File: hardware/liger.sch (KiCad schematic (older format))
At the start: 61 parts, among them P1 CONN_01X10, P2 CONN_01X10, P3 USB_OTG, P4 CONN_01X02, P5 CONN_01X04, Q1 Q_NMOS_GSD, Q2 Q_PMOS_GSD, Q3 Q_NPN_BEC, Q4 Q_NPN_BEC, SW1 SW_PUSH, U1 electret_microphone, U11 SPX3819, U2 ADA4075, U3 ESP-WROOM-02, U4 FT230XS, U5 PT5529B/L2/H2-F

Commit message: pcbebe
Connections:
- net at Relay1.8: now also P4.1 (P1)
- net at Relay1.9: no longer P4.1 (P1)

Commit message: almost done
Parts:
- removed R19: 100 something, Resistors_SMD:R_0603, symbol R
- R18: value 100something -> 1K; Part Number (none) -> RC0603JR-071KL
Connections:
- net +3V3: now also R18.1
- net RXD: now also R18.2, U4.1 (TXD); no longer R18.1
- net TXD: now also U4.4 (RXD)
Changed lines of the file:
@@
 Text GLabel 12100 4700 2    60   Input ~ 0
 RESET
-Text GLabel 12050 3950 2    60   Input ~ 0
+Text GLabel 11900 3950 2    60   Input ~ 0
 TXD
-Text GLabel 12050 3850 2    60   Input ~ 0
+Text GLabel 11600 3850 2    60   Input ~ 0
 RXD
 $Comp
@@
 $EndComp
 $Comp
-L R R18
-U 1 1 57701A9A
-P 11750 3850
-F 0 "R18" V 11650 3850 50  0000 C CNN
-F 1 "100something" V 11750 3850 50  0000 C CNN
-F 2 "Resistors_SMD:R_0603" V 11680 3850 50  0001 C CNN
-F 3 "" H 11750 3850 50  0000 C CNN
-	1    11750 3850
-	0    1    1    0
-$EndComp
-$Comp
-L R R19
-U 1 1 57701B37
-P 11750 3950
-F 0 "R19" V 11830 3950 50  0000 C CNN
-F 1 "100 something" V 11750 3950 50  0000 C CNN
-F 2 "Resistors_SMD:R_0603" V 11680 3950 50  0001 C CNN
-F 3 "" H 11750 3950 50  0000 C CNN
-	1    11750 3950
-	0    1    1    0
-$EndComp
-$Comp
 L C C2
 U 1 1 577082C5
@@
 Connection ~ 10750 4950
 Wire Wire Line
-	11450 3850 11600 3850
-Wire Wire Line
-	11450 3950 11600 3950
+	11450 3950 11900 3950
 Wire Wire Line
 	10650 3550 10650 3450
@@
 Connection ~ 10050 5200
 Wire Wire Line
-	10850 3300 9050 3300
+	9050 3300 10850 3300
 Wire Wire Line
 	9900 3850 9900 3300
 Connection ~ 9900 3300
-Wire Wire Line
-	11900 3850 12050 3850
-Wire Wire Line
-	11900 3950 12050 3950
 Wire Notes Line
 	13000 6250 500  6250
@@
 	6150 4450 6400 4450
 Wire Wire Line
-	6150 4350 6400 4350
-Wire Wire Line
 	6150 4250 6400 4250
-Wire Wire Line
-	6150 4150 6850 4150
 Text GLabel 6400 3950 2    60   Input ~ 0
 Reset
@@
 Text GLabel 6400 3750 2    60   Input ~ 0
 IO16
-Wire Wire Line
-	6850 4150 6850 4250
 $Comp
 L GND #PWR027
-U 1 1 57704840
-P 6850 4250
-F 0 "#PWR027" H 6850 4000 50  0001 C CNN
-F 1 "GND" H 6850 4100 50  0000 C CNN
-F 2 "" H 6850 4250 50  0000 C CNN
-F 3 "" H 6850 4250 50  0000 C CNN
-	1    6850 4250
-	1    0    0    -1
-$EndComp
-$Comp
-L GND #PWR028
 U 1 1 57704A85
 P 4800 4550
-F 0 "#PWR028" H 4800 4300 50  0001 C CNN
+F 0 "#PWR027" H 4800 4300 50  0001 C CNN
 F 1 "GND" H 4800 4400 50  0000 C CNN
 F 2 "" H 4800 4550 50  0000 C CNN
@@
 	4800 4550 4800 4450
 $Comp
-L +3.3V #PWR029
+L +3.3V #PWR028
 U 1 1 577051B4
 P 4800 3250
-F 0 "#PWR029" H 4800 3100 50  0001 C CNN
+F 0 "#PWR028" H 4800 3100 50  0001 C CNN
 F 1 "+3.3V" H 4800 3390 50  0000 C CNN
 F 2 "" H 4800 3250 50  0000 C CNN
@@
 	12050 1100 12050 1000
 $Comp
-L +5V #PWR030
+L +5V #PWR029
 U 1 1 5771C30D
 P 12050 1000
-F 0 "#PWR030" H 12050 850 50  0001 C CNN
+F 0 "#PWR029" H 12050 850 50  0001 C CNN
 F 1 "+5V" H 12050 1140 50  0000 C CNN
 F 2 "" H 12050 1000 50  0000 C CNN
@@
 $EndComp
 $Comp
-L GND #PWR031
+L GND #PWR030
 U 1 1 5771C669
 P 11750 1150
-F 0 "#PWR031" H 11750 900 50  0001 C CNN
+F 0 "#PWR030" H 11750 900 50  0001 C CNN
 F 1 "GND" H 11750 1000 50  0000 C CNN
 F 2 "" H 11750 1150 50  0000 C CNN
@@
 	12700 950  12700 1100
 $Comp
-L +5V #PWR032
+L +5V #PWR031
 U 1 1 57726F3B
 P 12700 950
-F 0 "#PWR032" H 12700 800 50  0001 C CNN
+F 0 "#PWR031" H 12700 800 50  0001 C CNN
 F 1 "+5V" H 12700 1090 50  0000 C CNN
 F 2 "" H 12700 950 50  0000 C CNN
@@
 	12700 2400 12700 2600
 $Comp
-L GND #PWR033
+L GND #PWR032
 U 1 1 57727DF2
 P 12700 2600
-F 0 "#PWR033" H 12700 2350 50  0001 C CNN
+F 0 "#PWR032" H 12700 2350 50  0001 C CNN
 F 1 "GND" H 12700 2450 50  0000 C CNN
 F 2 "" H 12700 2600 50  0000 C CNN
@@
 	6100 5200 6250 5200
 $Comp
-L GND #PWR034
+L GND #PWR033
 U 1 1 57744532
 P 6400 5000
-F 0 "#PWR034" H 6400 4750 50  0001 C CNN
+F 0 "#PWR033" H 6400 4750 50  0001 C CNN
 F 1 "GND" H 6400 4850 50  0000 C CNN
 F 2 "" H 6400 5000 50  0000 C CNN
@@
 $EndComp
 $Comp
-L +BATT #PWR035
+L +BATT #PWR034
 U 1 1 57744770
 P 6650 5100
-F 0 "#PWR035" H 6650 4950 50  0001 C CNN
+F 0 "#PWR034" H 6650 4950 50  0001 C CNN
 F 1 "+BATT" H 6650 5240 50  0000 C CNN
 F 2 "" H 6650 5100 50  0000 C CNN
@@
 $EndComp
 $Comp
-L +5V #PWR036
+L +5V #PWR035
 U 1 1 57744A7C
 P 6250 5200
-F 0 "#PWR036" H 6250 5050 50  0001 C CNN
+F 0 "#PWR035" H 6250 5050 50  0001 C CNN
 F 1 "+5V" H 6250 5340 50  0000 C CNN
 F 2 "" H 6250 5200 50  0000 C CNN
@@
 Connection ~ 4600 5050
 $Comp
-L GND #PWR037
+L GND #PWR036
 U 1 1 57746D84
 P 4550 5050
-F 0 "#PWR037" H 4550 4800 50  0001 C CNN
+F 0 "#PWR036" H 4550 4800 50  0001 C CNN
 F 1 "GND" H 4550 4900 50  0000 C CNN
 F 2 "" H 4550 5050 50  0000 C CNN
@@
 $EndComp
 $Comp
-L +3.3V #PWR038
+L +3.3V #PWR037
 U 1 1 57746FCF
 P 4600 5950
-F 0 "#PWR038" H 4600 5800 50  0001 C CNN
+F 0 "#PWR037" H 4600 5800 50  0001 C CNN
 F 1 "+3.3V" H 4600 6090 50  0000 C CNN
 F 2 "" H 4600 5950 50  0000 C CNN
@@
 $EndComp
 $Comp
-L +5V #PWR039
+L +5V #PWR038
 U 1 1 57758382
 P 7600 1050
-F 0 "#PWR039" H 7600 900 50  0001 C CNN
+F 0 "#PWR038" H 7600 900 50  0001 C CNN
 F 1 "+5V" H 7600 1190 50  0000 C CNN
 F 2 "" H 7600 1050 50  0000 C CNN
@@
 Wire Wire Line
 	9000 1650 9050 1650
+Wire Wire Line
+	6150 4150 6750 4150
+Wire Wire Line
+	6750 4150 6750 4200
+$Comp
+L R R18
+U 1 1 5776EAB6
+P 11550 3400
+F 0 "R18" V 11630 3400 50  0000 C CNN
+F 1 "1K" V 11550 3400 50  0000 C CNN
+F 2 "Resistors_SMD:R_0603" V 11480 3400 50  0001 C CNN
+F 3 "http://www.digikey.com/en/resources/datasheets/yageo/rc-series-l-suffix-datasheet" H 11550 3400 50  0001 C CNN
+F 4 "RC0603JR-071KL" V 11550 3400 60  0001 C CNN "Part Number"
+	1    11550 3400
+	1    0    0    -1
+$EndComp
+Wire Wire Line
+	11550 3250 11550 3150
+$Comp
+L +3.3V #PWR039
+U 1 1 5776EF57
+P 11550 3150
+F 0 "#PWR039" H 11550 3000 50  0001 C CNN
+F 1 "+3.3V" H 11550 3290 50  0000 C CNN
+F 2 "" H 11550 3150 50  0000 C CNN
+F 3 "" H 11550 3150 50  0000 C CNN
+	1    11550 3150
+	1    0    0    -1
+$EndComp
+Wire Wire Line
+	6150 4350 6400 4350
+Wire Wire Line
+	11600 3850 11450 3850
+$Comp
+L GND #PWR040
+U 1 1 57771C8C
+P 6750 4200
+F 0 "#PWR040" H 6750 3950 50  0001 C CNN
+F 1 "GND" H 6750 4050 50  0000 C CNN
+F 2 "" H 6750 4200 50  0000 C CNN
+F 3 "" H 6750 4200 50  0000 C CNN
+	1    6750 4200
+	1    0    0    -1
+$EndComp
+Wire Wire Line
+	11550 3550 11550 3850
+Connection ~ 11550 3850
 $EndSCHEMATC

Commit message: update
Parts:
- removed U3: ESP-WROOM-02, garage-opener:ESP-WROOM-02, symbol ESP-WROOM-02
- added U?: ESP-WROOM-02, symbol ESP-WROOM-02
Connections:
- net +BATT is gone; now on net +3V3: P2.9 (P9)
- net +3V3: now also U?.1 (3V3)
- net ADC: now also U?.16 (TOUT)
- net EN: now also U?.2 (EN)
- net GND: now also U?.13 (GND), U?.18 (GND), U?.9 (GND)
- net IO0: now also U?.8 (IO0)
- net IO12: now also U?.4 (IO12)
- net IO13: now also U?.5 (IO13)
- net IO14: now also U?.3 (IO14)
- net IO15: now also U?.6 (IO15)
- net IO16: now also U?.17 (IO16)
- net IO2: now also U?.7 (IO2)
- net IO4: now also U?.10 (IO4)
- net IO5: now also U?.14 (IO5)
- net RXD: now also U?.11 (RXD)
- net Reset: now also U?.15 (RST)
- net TXD: now also U?.12 (TXD)
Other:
- note added: "Automation\n & \nSecurity"
- note added: "Pyfi"

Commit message: errything
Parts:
- U3: renamed from U?; footprint (none) -> libraries:ESP-WROOM-02; Part Number (none) -> ESP-WROOM-02
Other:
- note added: "Technologies"
- note removed: "Automation\n & \nSecurity"

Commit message: final update
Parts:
- Relay1: footprint garage-opener:V23105 -> libraries:V23105
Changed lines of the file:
@@
 F 0 "Relay1" H 7750 1750 50  0000 L CNN
 F 1 "V23105" H 8850 1400 50  0000 L CNN
-F 2 "garage-opener:V23105" H 8400 1550 50  0001 C CNN
+F 2 "libraries:V23105" H 8400 1550 50  0001 C CNN
 F 3 "file:///home/chris/Downloads/ENG_SS_108-98007_L%20(3).pdf" H 8400 1550 50  0001 C CNN
 F 4 "V23105A5001A201" H 8400 1550 60  0001 C CNN "Part Number"

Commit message: update
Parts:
- FB1: value BK0603HS330-T -> BK1608HS330-T; Part Number BK0603HS330-T -> BK1608HS330-T
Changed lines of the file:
@@
 P 10250 3400
 F 0 "FB1" H 10350 3350 60  0000 C CNN
-F 1 "BK0603HS330-T" H 10400 3250 60  0000 C CNN
+F 1 "BK1608HS330-T" H 10400 3250 60  0000 C CNN
 F 2 "Resistors_SMD:R_0603" H 10250 3400 60  0001 C CNN
 F 3 "http://www.yuden.co.jp/productdata/catalog/en/mlci07_e.pdf" H 10250 3400 60  0001 C CNN
-F 4 "BK0603HS330-T" H 10250 3400 60  0001 C CNN "Part Number"
+F 4 "BK1608HS330-T" H 10250 3400 60  0001 C CNN "Part Number"
 	1    10250 3400
 	1    0    0    -1

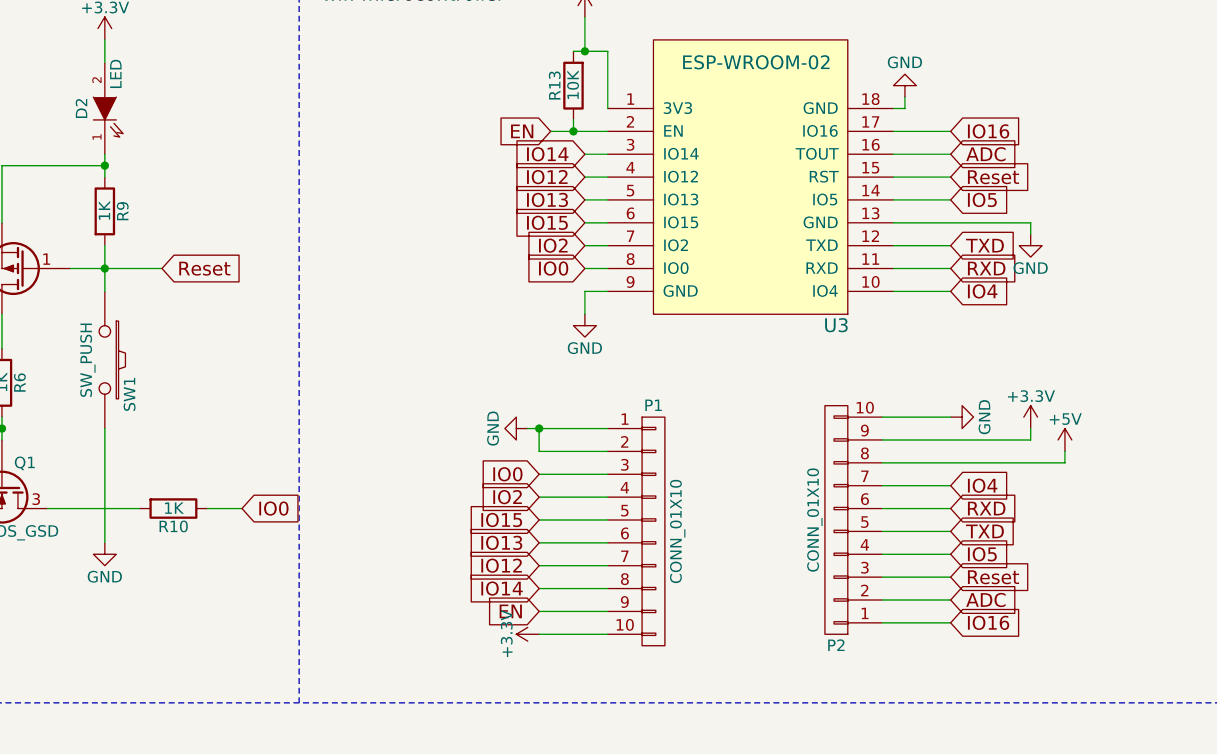
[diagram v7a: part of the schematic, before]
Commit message: fixed footprint errors, reorganized
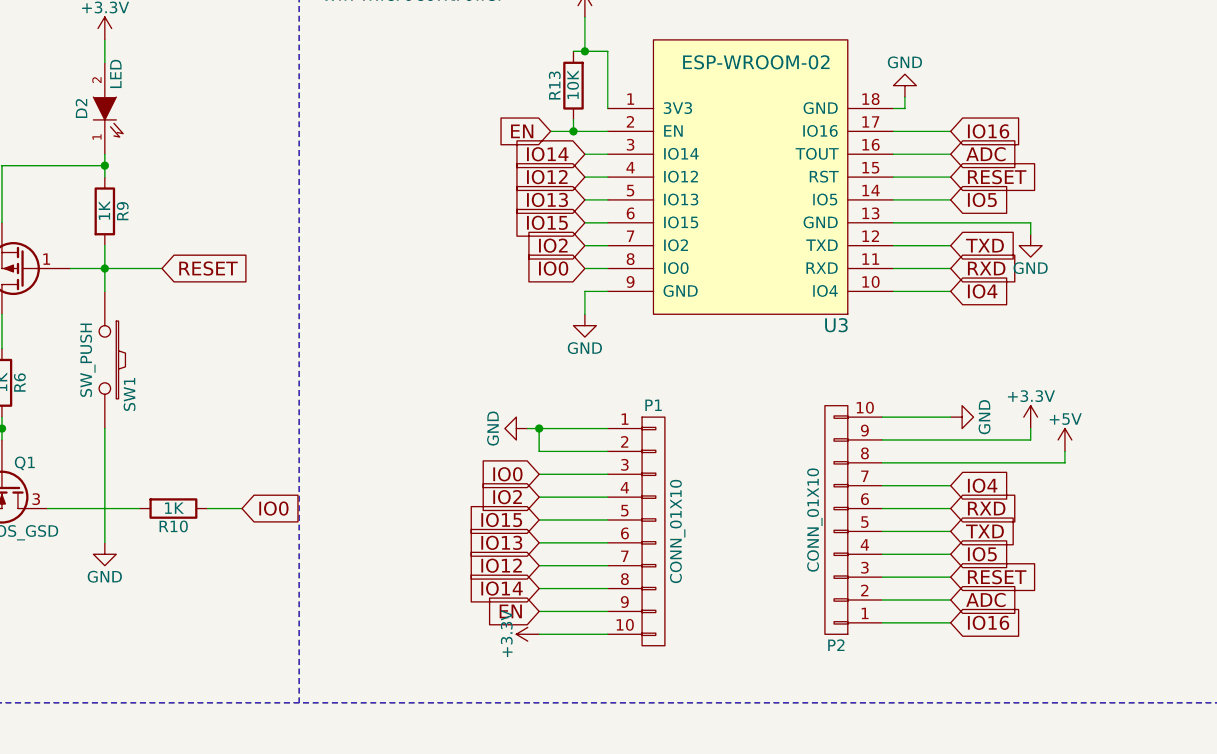
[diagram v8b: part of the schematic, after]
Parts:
- P3: footprint Connect:USB_Micro-B -> footprints:USB_Micro-B_CIRC
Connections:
- net Reset is gone; now on net RESET: P2.3 (P3), Q2.1 (G), R9.2, SW1.1, U3.15 (RST)
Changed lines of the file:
@@
 F 0 "P3" H 8625 4025 50  0000 C CNN
 F 1 "USB_OTG" H 8300 4350 50  0000 C CNN
-F 2 "Connect:USB_Micro-B" V 8250 4050 50  0001 C CNN
+F 2 "footprints:USB_Micro-B_CIRC" V 8250 4050 50  0001 C CNN
 F 3 "http://portal.fciconnect.com/Comergent//fci/drawing/10118194.pdf" V 8250 4050 50  0001 C CNN
 F 4 "10118194-0001LF" H 8300 4150 60  0001 C CNN "Part Number"
@@
 IO0
 Text GLabel 2950 4350 2    60   Input ~ 0
-Reset
+RESET
 $Comp
 L GND #PWR019
@@
 IO4
 Text GLabel 6400 3950 2    60   Input ~ 0
-Reset
+RESET
 Text GLabel 6400 5600 2    60   Input ~ 0
 IO5
@@
 ADC
 Text GLabel 6400 5700 2    60   Input ~ 0
-Reset
+RESET
 Text GLabel 6400 5900 2    60   Input ~ 0
 IO16
